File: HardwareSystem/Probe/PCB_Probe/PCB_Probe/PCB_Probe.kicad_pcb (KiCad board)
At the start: 2 copper layers, 240 x 35 mm, 32 parts, among them J1 Conn_01x15, J2 Conn_01x15, J3 Conn_01x02_Socket, J4 Conn_01x04_Pin, U1 TLC555xP, U2 LP2950CZ-3.0/NOPB

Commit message: updated ground plane footprint
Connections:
- net Pobe renamed Probe
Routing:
- net GND: track 223.3 -> 240.5 mm, vias 4 -> 8
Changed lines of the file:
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@@
   )
   (net 0 "")
-  (net 1 "Pobe")
+  (net 1 "Probe")
   (net 2 "A_Light")
   (net 3 "+9V")
@@
       (net 34 "Net-(U1-Q)") (pintype "passive"))
     (pad "2" thru_hole oval (at 10.16 0) (size 1.6 1.6) (drill 0.8) (layers "*.Cu" "*.Mask")
-      (net 1 "Pobe") (pintype "passive"))
+      (net 1 "Probe") (pintype "passive"))
     (model "${KICAD6_3DMODEL_DIR}/Resistor_THT.3dshapes/R_Axial_DIN0207_L6.3mm_D2.5mm_P10.16mm_Horizontal.wrl"
       (offset (xyz 0 0 0))
@@
       (net 7 "A_Moisture") (pinfunction "K") (pintype "passive"))
     (pad "2" thru_hole oval (at 7.62 0) (size 1.6 1.6) (drill 0.8) (layers "*.Cu" "*.Mask")
-      (net 1 "Pobe") (pinfunction "A") (pintype "passive"))
+      (net 1 "Probe") (pinfunction "A") (pintype "passive"))
     (model "${KICAD6_3DMODEL_DIR}/Diode_THT.3dshapes/D_DO-35_SOD27_P7.62mm_Horizontal.wrl"
       (offset (xyz 0 0 0))
@@
       (stroke (width 0.05) (type solid)) (fill none) (layer "F.CrtYd"))
     (pad "1" smd circle (at 0 0) (size 1 1) (layers "F.Cu" "F.Mask")
-      (net 1 "Pobe") (pinfunction "1") (pintype "passive"))
+      (net 1 "Probe") (pinfunction "1") (pintype "passive"))
   )
   (footprint "Resistor_THT:R_Axial_DIN0207_L6.3mm_D2.5mm_P10.16mm_Horizontal" (layer "F.Cu")
@@
     (property "ki_keywords" "LP2950CZ-3.0/NOPB")
     (attr through_hole)
-    (fp_text reference "U2" (at -0.254 -3.556 unlocked) (layer "F.SilkS")
+    (fp_text reference "U2" (at 1.27 0 unlocked) (layer "F.SilkS")
         (effects (font (size 1 1) (thickness 0.15)))
     )
@@
   (gr_text "APWS" (at 238.76 46.482) (layer "F.SilkS")
     (effects (font (size 2.5 2.5) (thickness 0.4) bold) (justify left bottom))
+  )
+  (dimension (type aligned) (layer "B.Cu")
+    (pts (xy 40 52.5) (xy 279.439144 52.525806))
+    (height 38.394392)
+    (gr_text "9.4267 in" (at 159.715628 89.107295 359.9938248) (layer "B.Cu")
+      (effects (font (size 1.5 1.5) (thickness 0.3)))
+    )
+    (format (prefix "") (suffix "") (units 3) (units_format 1) (precision 4))
+    (style (thickness 0.2) (arrow_length 1.27) (text_position_mode 0) (extension_height 0.58642) (extension_offset 0.5) keep_text_aligned)
+  )
+  (dimension (type aligned) (layer "B.Cu")
+    (pts (xy 192.998029 52.508297) (xy 280 52.5))
+    (height 26.611431)
+    (gr_text "3.4253 in" (at 236.501381 77.315579 0.005464708052) (layer "B.Cu")
+      (effects (font (size 1.5 1.5) (thickness 0.3)))
+    )
+    (format (prefix "") (suffix "") (units 3) (units_format 1) (precision 4))
+    (style (thickness 0.2) (arrow_length 1.27) (text_position_mode 0) (extension_height 0.58642) (extension_offset 0.5) keep_text_aligned)
+  )
+  (dimension (type aligned) (layer "B.Cu")
+    (pts (xy 260 70.000354) (xy 260 35))
+    (height 22.702)
+    (gr_text "1.3780 in" (at 280.902 52.500177 90) (layer "B.Cu")
+      (effects (font (size 1.5 1.5) (thickness 0.3)))
+    )
+    (format (prefix "") (suffix "") (units 3) (units_format 1) (precision 4))
+    (style (thickness 0.2) (arrow_length 1.27) (text_position_mode 0) (extension_height 0.58642) (extension_offset 0.5) keep_text_aligned)
   )
   (segment (start 186.182 54.102) (end 187.784 52.5) (width 0.25) (layer "F.Cu") (net 1))
@@
   (segment (start 89.949 54.864) (end 89.876 54.864) (width 0.25) (layer "F.Cu") (net 35))
   (segment (start 71.882 44.958) (end 76.454 40.386) (width 0.25) (layer "F.Cu") (net 35))
+  (via (at 192.278 46.99) (size 0.8) (drill 0.4) (layers "F.Cu" "B.Cu") (net 35))
+  (via (at 192.278 58.42) (size 0.8) (drill 0.4) (layers "F.Cu" "B.Cu") (net 35))
   (via (at 192.278 42.926) (size 0.8) (drill 0.4) (layers "F.Cu" "B.Cu") (net 35))
   (via (at 192.278 41.91) (size 0.8) (drill 0.4) (layers "F.Cu" "B.Cu") (net 35))
+  (via (at 192.278 45.72) (size 0.8) (drill 0.4) (layers "F.Cu" "B.Cu") (net 35))
+  (via (at 192.278 57.15) (size 0.8) (drill 0.4) (layers "F.Cu" "B.Cu") (net 35))
   (via (at 192.278 62.738) (size 0.8) (drill 0.4) (layers "F.Cu" "B.Cu") (free) (net 35))
   (via (at 192.278 61.722) (size 0.8) (drill 0.4) (layers "F.Cu" "B.Cu") (net 35))
   (segment (start 76.091 49.167) (end 88.751 49.167) (width 0.25) (layer "B.Cu") (net 35))
   (segment (start 177.17663 42.378) (end 171.958 47.59663) (width 0.25) (layer "B.Cu") (net 35))
+  (segment (start 189.738 43.18) (end 189.738 41.293) (width 0.25) (layer "B.Cu") (net 35))
   (segment (start 154.686 58.842) (end 99.06 58.842) (width 0.25) (layer "B.Cu") (net 35))
   (segment (start 88.751 49.167) (end 89.876 50.292) (width 0.25) (layer "B.Cu") (net 35))
   (segment (start 180.674 42.378) (end 181.142 41.91) (width 0.25) (layer "B.Cu") (net 35))
+  (segment (start 191.516 57.15) (end 192.278 57.15) (width 0.25) (layer "B.Cu") (net 35))
+  (segment (start 181.57 59.69) (end 188.976 59.69) (width 0.25) (layer "B.Cu") (net 35))
   (segment (start 174.528 52.568) (end 171.958 49.998) (width 0.25) (layer "B.Cu") (net 35))
   (segment (start 161.504 48.768) (end 161.036 49.236) (width 0.25) (layer "B.Cu") (net 35))
+  (segment (start 189.738 44.45) (end 189.738 43.18) (width 0.25) (layer "B.Cu") (net 35))
+  (segment (start 192.278 46.99) (end 189.738 44.45) (width 0.25) (layer "B.Cu") (net 35))
+  (segment (start 188.976 59.69) (end 189.992 59.69) (width 0.25) (layer "B.Cu") (net 35))
+  (segment (start 189.992 59.69) (end 191.008 59.69) (width 0.25) (layer "B.Cu") (net 35))
   (segment (start 179.792 55.312) (end 177.048 52.568) (width 0.25) (layer "B.Cu") (net 35))
   (segment (start 170.728 48.768) (end 161.504 48.768) (width 0.25) (layer "B.Cu") (net 35))
@@
   (segment (start 171.958 47.59663) (end 171.958 49.998) (width 0.25) (layer "B.Cu") (net 35))
   (segment (start 161.036 48.006) (end 157.988 44.958) (width 0.25) (layer "B.Cu") (net 35))
+  (segment (start 189.23 40.785) (end 182.267 40.785) (width 0.25) (layer "B.Cu") (net 35))
   (segment (start 157.988 52.07) (end 157.988 48.514) (width 0.25) (layer "B.Cu") (net 35))
   (segment (start 177.048 52.568) (end 174.528 52.568) (width 0.25) (layer "B.Cu") (net 35))
   (segment (start 89.876 54.791) (end 89.876 54.356) (width 0.25) (layer "B.Cu") (net 35))
   (segment (start 71.882 44.958) (end 76.091 49.167) (width 0.25) (layer "B.Cu") (net 35))
-  (segment (start 190.754 40.785) (end 182.267 40.785) (width 0.25) (layer "B.Cu") (net 35))
+  (segment (start 192.278 58.42) (end 191.008 59.69) (width 0.25) (layer "B.Cu") (net 35))
+  (segment (start 190.754 40.785) (end 189.23 40.785) (width 0.25) (layer "B.Cu") (net 35))
   (segment (start 192.278 42.926) (end 190.137 40.785) (width 0.25) (layer "B.Cu") (net 35))
   (segment (start 192.278 61.722) (end 192.278 60.706) (width 0.25) (layer "B.Cu") (net 35))
@@
   (segment (start 155.28 58.842) (end 154.686 58.842) (width 0.25) (layer "B.Cu") (net 35))
   (segment (start 190.137 40.785) (end 189.992 40.785) (width 0.25) (layer "B.Cu") (net 35))
+  (segment (start 191.008 59.69) (end 191.262 59.69) (width 0.25) (layer "B.Cu") (net 35))
   (segment (start 89.876 50.292) (end 89.876 54.864) (width 0.25) (layer "B.Cu") (net 35))
-  (segment (start 181.57 59.69) (end 189.992 59.69) (width 0.25) (layer "B.Cu") (net 35))
+  (segment (start 192.278 45.72) (end 189.738 43.18) (width 0.25) (layer "B.Cu") (net 35))
   (segment (start 179.792 61.468) (end 181.57 59.69) (width 0.25) (layer "B.Cu") (net 35))
   (segment (start 159.268 63.424) (end 154.686 58.842) (width 0.25) (layer "B.Cu") (net 35))
@@
   (segment (start 157.988 52.07) (end 158.202 52.07) (width 0.25) (layer "B.Cu") (net 35))
   (segment (start 157.988 56.134) (end 157.988 52.07) (width 0.25) (layer "B.Cu") (net 35))
+  (segment (start 188.976 59.69) (end 191.516 57.15) (width 0.25) (layer "B.Cu") (net 35))
   (segment (start 179.792 61.468) (end 179.792 55.312) (width 0.25) (layer "B.Cu") (net 35))
-  (segment (start 189.992 59.69) (end 191.262 59.69) (width 0.25) (layer "B.Cu") (net 35))
   (segment (start 192.278 62.738) (end 191.516 61.976) (width 0.25) (layer "B.Cu") (net 35))
+  (segment (start 189.738 41.293) (end 189.23 40.785) (width 0.25) (layer "B.Cu") (net 35))
   (segment (start 182.267 40.785) (end 181.142 41.91) (width 0.25) (layer "B.Cu") (net 35))
   (segment (start 159.268 67.31) (end 159.268 63.424) (width 0.25) (layer "B.Cu") (net 35))
@@
     (polygon
       (pts
-        (xy 191.516 40.132)
-        (xy 263.398 40.132)
-        (xy 277.622 52.578)
-        (xy 263.652 64.262)
-        (xy 191.51742 64.607202)
-        (xy 191.516 60.96)
-        (xy 193.04 60.96)
-        (xy 263.144 60.96)
-        (xy 274.574 52.578)
-        (xy 263.398 43.434)
-        (xy 191.516 43.434)
+        (xy 191.008 35.56)
+        (xy 191.008 69.596)
+        (xy 259.842 69.596)
+        (xy 279.439144 52.525806)
+        (xy 259.842 35.56)
+        (xy 191.262 35.56)
       )
     )

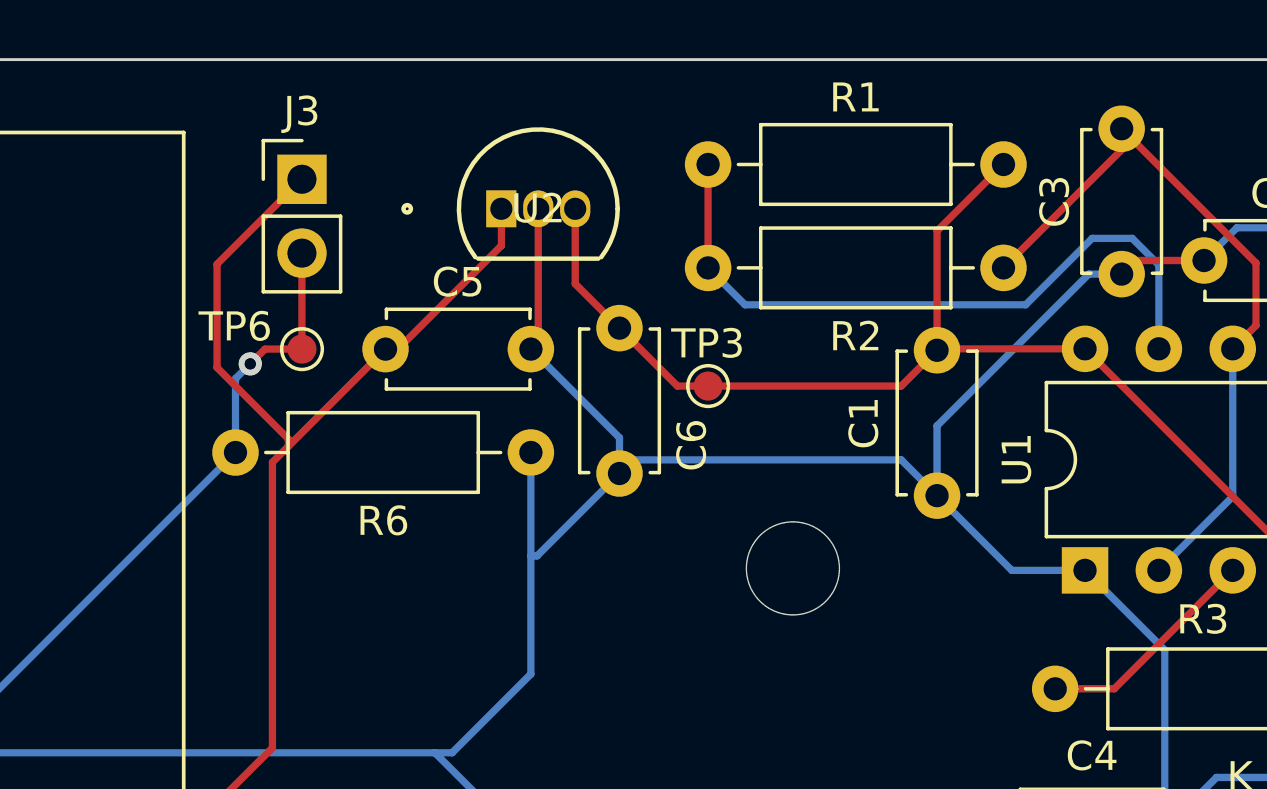
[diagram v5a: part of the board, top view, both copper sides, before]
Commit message: removed redundant 3V LDO
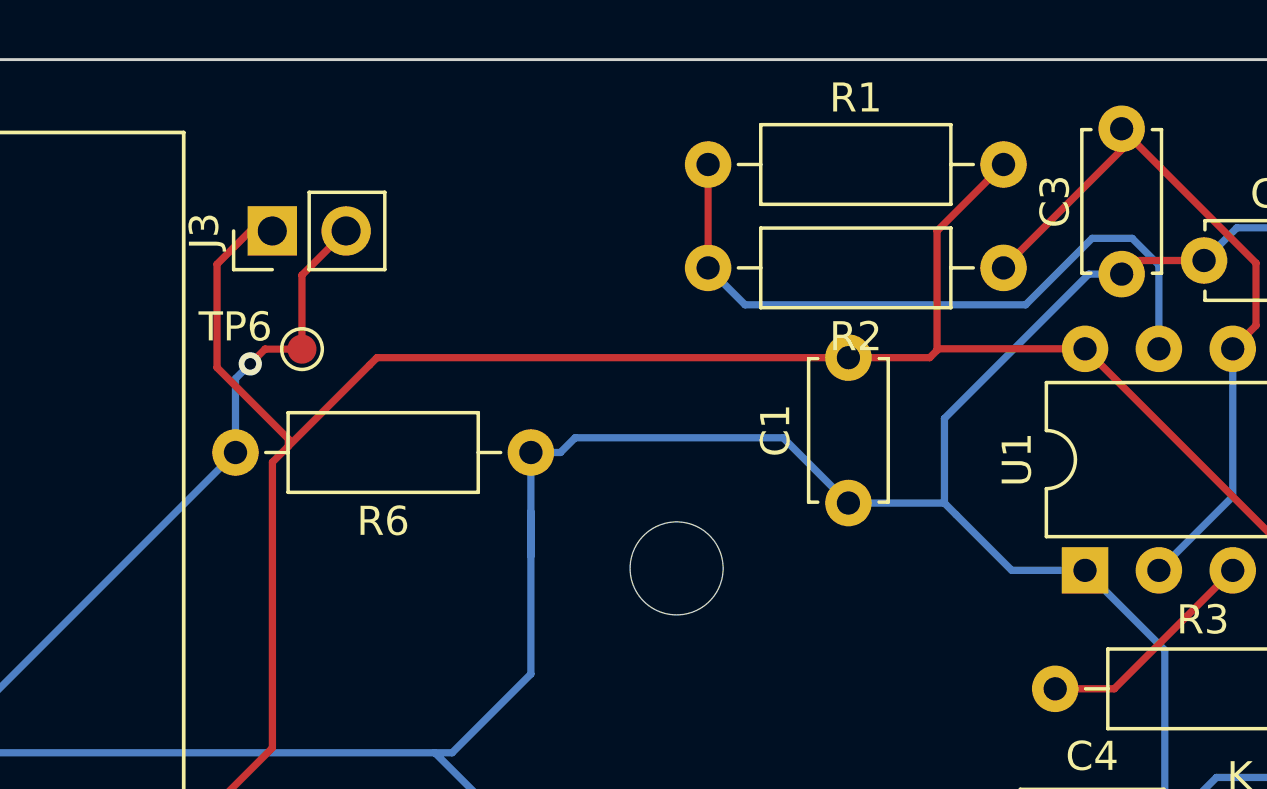
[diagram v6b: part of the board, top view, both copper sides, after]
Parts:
- removed C5: 4.7uF, Capacitor_THT:C_Disc_D4.7mm_W2.5mm_P5.00mm
- removed C6: 1uF, Capacitor_THT:C_Disc_D4.7mm_W2.5mm_P5.00mm
- removed TP3: 3V Testpoint, TestPoint:TestPoint_Pad_D1.0mm
- removed U2: LP2950CZ-3.0/NOPB, KiCADv6:Z03A_TEX
- moved H5 4.00 mm to (163.0, 52.5)
- moved C1 3.06 mm to (168.9, 50.3)
- moved J3 2.05 mm to (149.1, 40.9), turned to 90 degrees
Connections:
- C1 pad 2: +3V0 -> +3.3V
- R1 pad 1: +3V0 -> +3.3V
- U1 pad 4: +3V0 -> +3.3V
- U1 pad 8: +3V0 -> +3.3V
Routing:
- net +3V0: track 40.2 -> 0.00 mm
- net +3.3V: track 156.8 -> 190.5 mm
- net GND: track 240.5 -> 230.8 mm
- net A_Light: track 107.1 -> 108.5 mm

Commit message: updates on both boards
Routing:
- net GND: track 230.8 -> 229.3 mm
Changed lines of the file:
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@@
     (property "ki_keywords" "R res resistor")
     (attr through_hole)
-    (fp_text reference "R2" (at 5.08 -2.37 180) (layer "F.SilkS")
+    (fp_text reference "R2" (at 7.874 -2.37 180) (layer "F.SilkS")
         (effects (font (size 1 1) (thickness 0.15)))
     )
@@
   (gr_text "APWS" (at 238.76 46.482) (layer "F.SilkS")
     (effects (font (size 2.5 2.5) (thickness 0.4) bold) (justify left bottom))
-  )
-  (dimension (type aligned) (layer "B.Cu")
-    (pts (xy 192.998029 52.508297) (xy 280 52.5))
-    (height 26.611431)
-    (gr_text "87.0020 mm" (at 236.501381 77.315579 0.005464708052) (layer "B.Cu")
-      (effects (font (size 1.5 1.5) (thickness 0.3)))
-    )
-    (format (prefix "") (suffix "") (units 3) (units_format 1) (precision 4))
-    (style (thickness 0.2) (arrow_length 1.27) (text_position_mode 0) (extension_height 0.58642) (extension_offset 0.5) keep_text_aligned)
   )
   (dimension (type aligned) (layer "Dwgs.User")
@@
   (segment (start 174.528 52.568) (end 172.613 50.653) (width 0.25) (layer "B.Cu") (net 34))
   (segment (start 180.674 42.378) (end 181.142 41.91) (width 0.25) (layer "B.Cu") (net 34))
-  (segment (start 191.516 57.15) (end 192.278 57.15) (width 0.25) (layer "B.Cu") (net 34))
   (segment (start 181.57 59.69) (end 188.976 59.69) (width 0.25) (layer "B.Cu") (net 34))
   (segment (start 166.664 48.006) (end 159.512 48.006) (width 0.25) (layer "B.Cu") (net 34))
   (segment (start 178.308 42.378) (end 177.17663 42.378) (width 0.25) (layer "B.Cu") (net 34))
-  (segment (start 189.738 44.45) (end 189.738 43.18) (width 0.25) (layer "B.Cu") (net 34))
-  (segment (start 192.278 46.99) (end 189.738 44.45) (width 0.25) (layer "B.Cu") (net 34))
+  (segment (start 191.516 57.15) (end 188.976 59.69) (width 0.25) (layer "B.Cu") (net 34))
+  (segment (start 190.137 40.785) (end 189.992 40.785) (width 0.25) (layer "B.Cu") (net 34))
   (segment (start 188.976 59.69) (end 189.992 59.69) (width 0.25) (layer "B.Cu") (net 34))
+  (segment (start 191.516 61.976) (end 191.516 60.96) (width 0.25) (layer "B.Cu") (net 34))
   (segment (start 189.992 59.69) (end 191.008 59.69) (width 0.25) (layer "B.Cu") (net 34))
   (segment (start 179.792 55.312) (end 177.048 52.568) (width 0.25) (layer "B.Cu") (net 34))
+  (segment (start 192.278 46.99) (end 189.738 44.45) (width 0.25) (layer "B.Cu") (net 34))
   (segment (start 172.212 47.34263) (end 172.212 50.252) (width 0.25) (layer "B.Cu") (net 34))
-  (segment (start 191.153 40.785) (end 190.754 40.785) (width 0.25) (layer "B.Cu") (net 34))
+  (segment (start 189.738 44.45) (end 189.738 43.18) (width 0.25) (layer "B.Cu") (net 34))
+  (segment (start 192.278 61.722) (end 192.278 60.706) (width 0.25) (layer "B.Cu") (net 34))
   (segment (start 168.91 50.252) (end 166.664 48.006) (width 0.25) (layer "B.Cu") (net 34))
+  (segment (start 155.28 58.842) (end 157.988 56.134) (width 0.25) (layer "B.Cu") (net 34))
   (segment (start 189.23 40.785) (end 182.267 40.785) (width 0.25) (layer "B.Cu") (net 34))
-  (segment (start 157.988 52.07) (end 157.988 48.514) (width 0.25) (layer "B.Cu") (net 34))
+  (segment (start 192.278 60.706) (end 191.262 59.69) (width 0.25) (layer "B.Cu") (net 34))
   (segment (start 177.048 52.568) (end 174.528 52.568) (width 0.25) (layer "B.Cu") (net 34))
+  (segment (start 192.278 62.738) (end 191.516 61.976) (width 0.25) (layer "B.Cu") (net 34))
   (segment (start 89.876 54.791) (end 89.876 54.356) (width 0.25) (layer "B.Cu") (net 34))
   (segment (start 71.882 44.958) (end 76.091 49.167) (width 0.25) (layer "B.Cu") (net 34))
   (segment (start 159.512 48.006) (end 159.004 48.514) (width 0.25) (layer "B.Cu") (net 34))
+  (segment (start 191.516 60.96) (end 190.246 59.69) (width 0.25) (layer "B.Cu") (net 34))
+  (segment (start 192.278 57.15) (end 191.516 57.15) (width 0.25) (layer "B.Cu") (net 34))
+  (segment (start 168.91 50.252) (end 172.212 50.252) (width 0.25) (layer "B.Cu") (net 34))
+  (segment (start 89.876 50.292) (end 89.876 54.864) (width 0.25) (layer "B.Cu") (net 34))
   (segment (start 192.278 58.42) (end 191.008 59.69) (width 0.25) (layer "B.Cu") (net 34))
-  (segment (start 190.754 40.785) (end 189.23 40.785) (width 0.25) (layer "B.Cu") (net 34))
-  (segment (start 192.278 42.926) (end 190.137 40.785) (width 0.25) (layer "B.Cu") (net 34))
-  (segment (start 192.278 61.722) (end 192.278 60.706) (width 0.25) (layer "B.Cu") (net 34))
-  (segment (start 155.28 58.842) (end 157.988 56.134) (width 0.25) (layer "B.Cu") (net 34))
-  (segment (start 155.28 58.842) (end 154.686 58.842) (width 0.25) (layer "B.Cu") (net 34))
-  (segment (start 168.91 50.252) (end 172.212 50.252) (width 0.25) (layer "B.Cu") (net 34))
-  (segment (start 190.137 40.785) (end 189.992 40.785) (width 0.25) (layer "B.Cu") (net 34))
-  (segment (start 157.988 52.07) (end 157.988 50.546) (width 0.25) (layer "B.Cu") (net 34))
-  (segment (start 191.008 59.69) (end 191.262 59.69) (width 0.25) (layer "B.Cu") (net 34))
-  (segment (start 89.876 50.292) (end 89.876 54.864) (width 0.25) (layer "B.Cu") (net 34))
-  (segment (start 192.278 45.72) (end 189.738 43.18) (width 0.25) (layer "B.Cu") (net 34))
   (segment (start 179.792 61.468) (end 181.57 59.69) (width 0.25) (layer "B.Cu") (net 34))
   (segment (start 159.268 63.424) (end 154.686 58.842) (width 0.25) (layer "B.Cu") (net 34))
   (segment (start 159.004 48.514) (end 157.988 48.514) (width 0.25) (layer "B.Cu") (net 34))
+  (segment (start 99.06 58.842) (end 93.927 58.842) (width 0.25) (layer "B.Cu") (net 34))
+  (segment (start 157.988 56.134) (end 157.988 48.514) (width 0.25) (layer "B.Cu") (net 34))
+  (segment (start 192.278 45.72) (end 189.738 43.18) (width 0.25) (layer "B.Cu") (net 34))
+  (segment (start 192.278 42.926) (end 190.137 40.785) (width 0.25) (layer "B.Cu") (net 34))
+  (segment (start 191.262 59.69) (end 191.008 59.69) (width 0.25) (layer "B.Cu") (net 34))
   (segment (start 192.278 41.91) (end 191.153 40.785) (width 0.25) (layer "B.Cu") (net 34))
-  (segment (start 99.06 58.842) (end 93.927 58.842) (width 0.25) (layer "B.Cu") (net 34))
-  (segment (start 191.516 61.976) (end 191.516 60.96) (width 0.25) (layer "B.Cu") (net 34))
   (segment (start 190.246 59.69) (end 189.992 59.69) (width 0.25) (layer "B.Cu") (net 34))
-  (segment (start 191.516 60.96) (end 190.246 59.69) (width 0.25) (layer "B.Cu") (net 34))
-  (segment (start 192.278 60.706) (end 191.262 59.69) (width 0.25) (layer "B.Cu") (net 34))
-  (segment (start 157.988 56.134) (end 157.988 52.07) (width 0.25) (layer "B.Cu") (net 34))
-  (segment (start 188.976 59.69) (end 191.516 57.15) (width 0.25) (layer "B.Cu") (net 34))
   (segment (start 177.17663 42.378) (end 172.212 47.34263) (width 0.25) (layer "B.Cu") (net 34))
   (segment (start 179.792 61.468) (end 179.792 55.312) (width 0.25) (layer "B.Cu") (net 34))
-  (segment (start 192.278 62.738) (end 191.516 61.976) (width 0.25) (layer "B.Cu") (net 34))
+  (segment (start 191.153 40.785) (end 189.23 40.785) (width 0.25) (layer "B.Cu") (net 34))
+  (segment (start 154.686 58.842) (end 155.28 58.842) (width 0.25) (layer "B.Cu") (net 34))
   (segment (start 189.738 41.293) (end 189.23 40.785) (width 0.25) (layer "B.Cu") (net 34))
   (segment (start 182.267 40.785) (end 181.142 41.91) (width 0.25) (layer "B.Cu") (net 34))
